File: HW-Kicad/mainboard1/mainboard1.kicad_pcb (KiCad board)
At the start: 2 copper layers, 33.6 x 63.4 mm, 1 part, among them M1 LightAPRS

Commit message: comienzo mainboard
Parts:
- removed M1: LightAPRS, LightAPRS:LightAPRS
- added J1: Conn_01x02_Male, Connector_Molex:Molex_KK-254_AE-6410-02A_1x02_P2.54mm_Vertical, F.Cu at (132.6, 59.7)
- added J2: Conn_01x02_Male, Connector_PinHeader_2.54mm:PinHeader_1x02_P2.54mm_Horizontal, F.Cu at (128.7, 69.5)
- added J3: Conn_01x07_Male, Connector_PinHeader_2.54mm:PinHeader_1x07_P2.54mm_Horizontal, F.Cu at (128.9, 91.8)
- added J4: Conn_01x04_Male, Connector_Molex:Molex_KK-254_AE-6410-04A_1x04_P2.54mm_Vertical, B.Cu at (144.5, 47.1)
- added J5: Conn_01x04_Male, Connector_Molex:Molex_KK-254_AE-6410-04A_1x04_P2.54mm_Vertical, B.Cu at (198.1, 46.3)
- added U1: ESP32-DevKitC, espressif:ESP32-DevKitC, F.Cu at (155.6, 48.3)
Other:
- board size 33.6 x 63.4 mm -> 101 x 101 mm

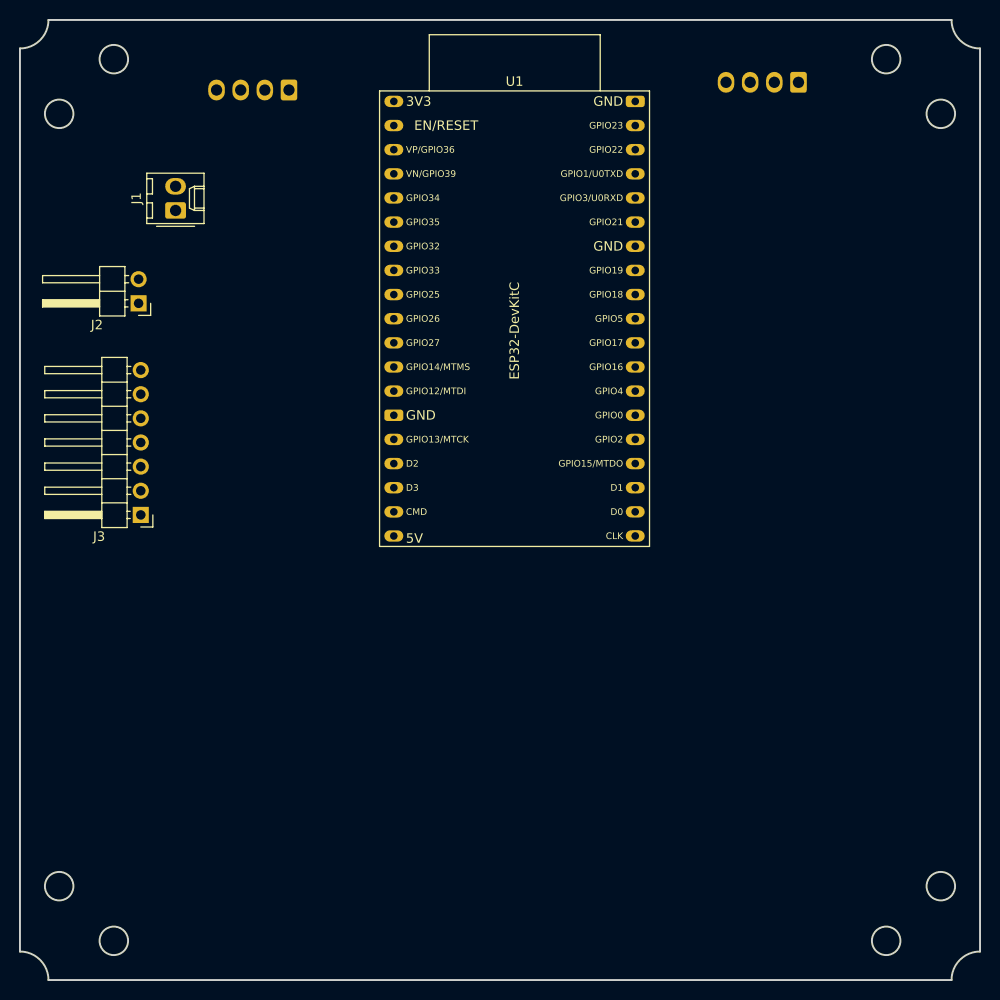
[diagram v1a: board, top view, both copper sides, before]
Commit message: cambio de footprint esp32 y ruteo de algunas pistas
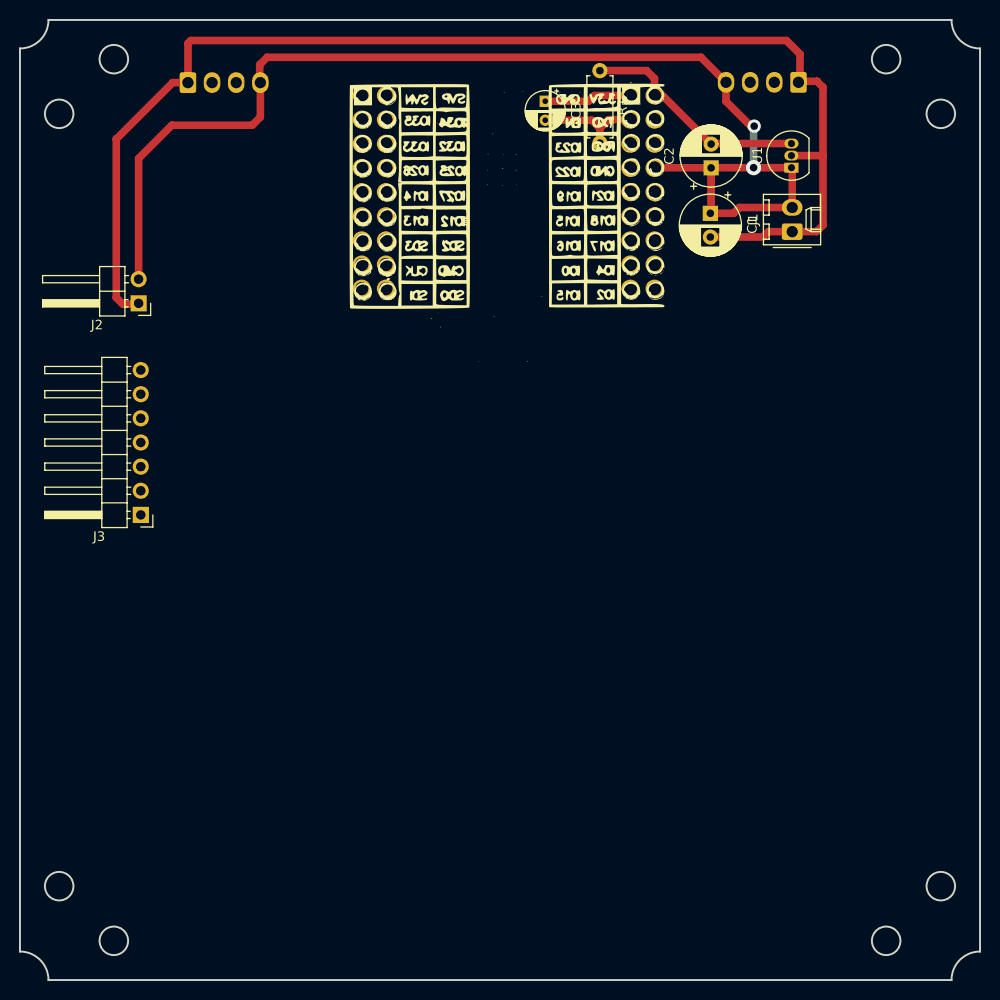
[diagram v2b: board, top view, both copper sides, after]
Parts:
- added C1: 100u, Capacitor_THT:CP_Radial_D6.3mm_P2.50mm, F.Cu at (188.9, 60.0)
- added C2: 100u, Capacitor_THT:CP_Radial_D6.3mm_P2.50mm, F.Cu at (188.9, 55.3)
- added C3: 10u, Capacitor_THT:CP_Radial_D4.0mm_P2.00mm, F.Cu at (171.5, 48.2)
- added R1: 10k, Resistor_THT:R_Axial_DIN0207_L6.3mm_D2.5mm_P7.62mm_Horizontal, F.Cu at (177.2, 45.0)
- added U2: ESP32-WROOM-E, ESP32:esp32_breakout, F.Cu at (168.3, 57.0)
- U1: value ESP32-DevKitC -> MCP1700-2802E_TO92; footprint espressif:ESP32-DevKitC -> Package_TO_SOT_THT:TO-92_Inline
- moved J1 64.9 mm to (197.5, 62.0)
- moved U1 42.4 mm to (197.4, 55.2), turned to 90 degrees
- moved J4 10.7 mm to (133.9, 46.3), turned to 0 degrees
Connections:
- U1 pad 1: unconnected-(U1-Pad1) -> GND
- U1 pad 2: unconnected-(U1-Pad2) -> VBAT
- U1 pad 3: unconnected-(U1-Pad3) -> 3V3
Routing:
- net GND: track 0.00 -> 135.3 mm, vias 0 -> 2
- net VBAT: track 0.00 -> 134.7 mm
- net 3V3: track 0.00 -> 24.5 mm
- net Net-(C3-Pad2): track 0.00 -> 11.2 mm

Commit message: falta agregar el mosfet que revienta el globo y el dtmf
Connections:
- U2 pad 13: unconnected-(U2-Pad13) -> MOSI
- U2 pad 14: unconnected-(U2-Pad14) -> SCK
- U2 pad 16: unconnected-(U2-Pad16) -> MISO
- U2 pad 30: unconnected-(U2-Pad30) -> PAYLOAD2RX
- U2 pad 33: unconnected-(U2-Pad33) -> PAYLOAD2TX
- U2 pad 7: unconnected-(U2-Pad7) -> PAYLOAD1TX
- U2 pad 9: unconnected-(U2-Pad9) -> PAYLOAD1RX
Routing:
- net SCK: track 0.00 -> 45.9 mm
- net MISO: track 0.00 -> 32.5 mm
- net MOSI: track 0.00 -> 32.2 mm
- net PAYLOAD2RX: track 0.00 -> 24.7 mm
- net PAYLOAD1RX: track 0.00 -> 20.1 mm
- net PAYLOAD2TX: track 0.00 -> 19.6 mm
- net PAYLOAD1TX: track 0.00 -> 16.2 mm

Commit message: agregue circuito de rotura de globo
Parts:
- added J6: Screw_Terminal_01x02, TerminalBlock:TerminalBlock_bornier-2_P5.08mm, F.Cu at (207.9, 100.8)
- added J7: Screw_Terminal_01x02, TerminalBlock:TerminalBlock_bornier-2_P5.08mm, F.Cu at (208.2, 64.7)
- added Q1: ATP213, Package_TO_SOT_SMD:TO-252-2, F.Cu at (206.2, 87.4)
- added Q2: ATP213, Package_TO_SOT_SMD:TO-252-2, F.Cu at (206.3, 79.0)
- added R2: 100k, Resistor_THT:R_Axial_DIN0207_L6.3mm_D2.5mm_P7.62mm_Horizontal, F.Cu at (198.8, 87.6)
- added R3: 100k, Resistor_THT:R_Axial_DIN0207_L6.3mm_D2.5mm_P7.62mm_Horizontal, F.Cu at (198.8, 79.0)
- J1: value Conn_01x02_Male -> Conn_01x03_Male; footprint Connector_Molex:Molex_KK-254_AE-6410-02A_1x02_P2.54mm_Vertical -> Connector_Molex:Molex_KK-254_AE-6410-03A_1x03_P2.54mm_Vertical
- moved J1 2.54 mm to (197.5, 64.5)
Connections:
- J1 pad 1: VBAT -> BAT++
- J1 pad 2: GND -> VBAT
- U2 pad 37: unconnected-(U2-Pad37) -> Net-(U2-Pad37)
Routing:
- net Net-(U2-Pad37): track 0.00 -> 69.3 mm, vias 0 -> 1
- net BAT++: track 0.00 -> 46.5 mm
- net GND: track 135.3 -> 161.7 mm
- net Net-(J7-Pad2): track 0.00 -> 9.60 mm
- net Net-(J6-Pad2): track 0.00 -> 8.53 mm
- added copper zone on F.Cu, net BAT++
- added copper zone on F.Cu, net GND
- added copper zone on F.Cu, net Net-(J6-Pad2)
- added copper zone on F.Cu, net Net-(J7-Pad2)

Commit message: cosas en mainboard
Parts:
- added C4: 100uF, Capacitor_THT:CP_Radial_D4.0mm_P2.00mm, F.Cu at (164.2, 89.1)
- added J8: Conn_02x10_Odd_Even, Connector_PinSocket_2.00mm:PinSocket_2x10_P2.00mm_Vertical, F.Cu at (143.3, 105.3)
- added REF**: 9xtend, 9xtend:9xtend, F.Cu at (142.0, 114.3)
- added U3: Mini360, mini360:Mini360_step-down, F.Cu at (149.1, 87.6)
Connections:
- U2 pad 13: MOSI -> unconnected-(U2-Pad13)
- U2 pad 14: SCK -> unconnected-(U2-Pad14)
- U2 pad 16: MISO -> unconnected-(U2-Pad16)
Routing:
- net unconnected-(U2-Pad13): track 0.00 -> 32.2 mm
- net MOSI: track 32.2 -> 0.00 mm

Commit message: mainboard terminada
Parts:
- removed J6, J7: Screw_Terminal_01x02, TerminalBlock:TerminalBlock_bornier-2_P5.08mm
- removed Q1, Q2: ATP213, Package_TO_SOT_SMD:TO-252-2
- removed R2, R3: 100k, Resistor_THT:R_Axial_DIN0207_L6.3mm_D2.5mm_P7.62mm_Horizontal
- added REF**: LightAPRS, LightAPRS:LightAPRS, F.Cu at (128.8, 71.7)
- added U4: YAAJ_DCDC_StepDown_LM2596, lm2596:DC_DC_LM2596_small, F.Cu at (167.8, 52.4)
- moved C4 50.6 mm to (128.4, 124.8), turned to 0 degrees
- moved U3 34.4 mm to (125.9, 113.0), turned to -90 degrees
- moved J8 25.7 mm to (136.8, 130.2), turned to 180 degrees
- moved U2 25.0 mm to (168.3, 82.0)
- moved R1 24.7 mm to (183.0, 69.0), turned to 180 degrees
- moved C3 24.6 mm to (174.5, 72.6)
- moved U1 20.4 mm to (197.3, 75.7)
- moved C1 19.2 mm to (189.8, 79.2), turned to 90 degrees
- moved C2 16.8 mm to (189.9, 72.1)
- moved J3 8.46 mm to (127.6, 83.4)
- moved REF** 7.95 mm to (137.7, 121.0)
- moved J1 7.68 mm to (204.3, 68.1), turned to -90 degrees
- moved J2 6.32 mm to (127.5, 63.3)
- moved J4 5.34 mm to (136.0, 51.2), turned to 90 degrees
- moved J5 2.99 mm to (199.5, 43.6), turned to -90 degrees
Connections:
- J1 pad 2: VBAT -> abortSig
- J3 pad 2: RST -> unconnected-(J3-Pad2)
- J3 pad 5: SCK -> unconnected-(J3-Pad5)
- J3 pad 6: MISO -> unconnected-(J3-Pad6)
- J3 pad 7: MOSI -> unconnected-(J3-Pad7)
- U2 pad 10: unconnected-(U2-Pad10) -> xtendTX
- U2 pad 11: unconnected-(U2-Pad11) -> SDA
- U2 pad 12: unconnected-(U2-Pad12) -> xtendPWR
- U2 pad 13: unconnected-(U2-Pad13) -> SCL
- U2 pad 16: unconnected-(U2-Pad16) -> xtendRX
- U2 pad 37: Net-(Q1-Pad1) -> abortSig
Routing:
- net VBAT: track 134.7 -> 240.8 mm, vias 0 -> 1
- net xtendTX: track 0.00 -> 70.0 mm
- net Net-(Q1-Pad1): track 69.3 -> 0.00 mm, vias 1 -> 0
- net xtendPWR: track 0.00 -> 67.8 mm
- net xtendRX: track 0.00 -> 56.4 mm
- net abortSig: track 0.00 -> 55.0 mm
- net PAYLOAD2RX: track 24.7 -> 74.7 mm
- net PAYLOAD2TX: track 19.6 -> 66.6 mm
- net SCK: track 45.9 -> 0.00 mm
- net PAYLOAD1TX: track 16.2 -> 49.0 mm
- net MISO: track 32.5 -> 0.00 mm
- net unconnected-(U2-Pad13): track 32.2 -> 0.00 mm
- net Net-(C4-Pad1): track 0.00 -> 28.3 mm
- net BAT++: track 46.5 -> 18.4 mm
- net GND: track 161.7 -> 189.4 mm
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- added copper zone on B.Cu, net GND
- removed copper zone on F.Cu, net BAT++
- removed copper zone on F.Cu, net GND
- removed copper zone on F.Cu, net Net-(J6-Pad2)
- removed copper zone on F.Cu, net Net-(J7-Pad2)
